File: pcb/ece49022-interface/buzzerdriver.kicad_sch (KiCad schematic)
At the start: 4 parts, among them Q1 C1815

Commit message: Interface
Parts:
- Q1: value C1815 -> KSC1815
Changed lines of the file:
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@@
 			)
 		)
-		(property "Value" "C1815"
+		(property "Value" "KSC1815"
 			(at 130.81 110.4899 0)
 			(effects
@@
 			)
 		)
-		(property "Description" "5399-C1815CT-ND"
+		(property "Description" "KSC1815YTA"
 			(at 125.73 109.22 0)
 			(effects

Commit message: footprint update
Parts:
- R2, R3: footprint (none) -> Resistor_SMD:R_0402_1005Metric
- renumbered Buzzer to Buzzer1
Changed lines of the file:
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@@
 		(dnp no)
 		(fields_autoplaced yes)
-		(property "Reference" "Buzzer"
+		(property "Reference" "Buzzer1"
 			(at 152.4 90.1699 90)
 			(effects
@@
 			(project "ece49022-interface"
 				(path "/ad062fbe-cbe6-4ffd-876d-97a59a1c7176/6d9997a2-880e-441e-bac1-2563afa1369d"
-					(reference "Buzzer")
+					(reference "Buzzer1")
 					(unit 1)
 				)
@@
 			)
 		)
-		(property "Footprint" ""
+		(property "Footprint" "Resistor_SMD:R_0402_1005Metric"
 			(at 127.254 91.186 90)
 			(effects
@@
 			)
 		)
-		(property "Footprint" ""
+		(property "Footprint" "Resistor_SMD:R_0402_1005Metric"
 			(at 108.204 108.204 90)
 			(effects

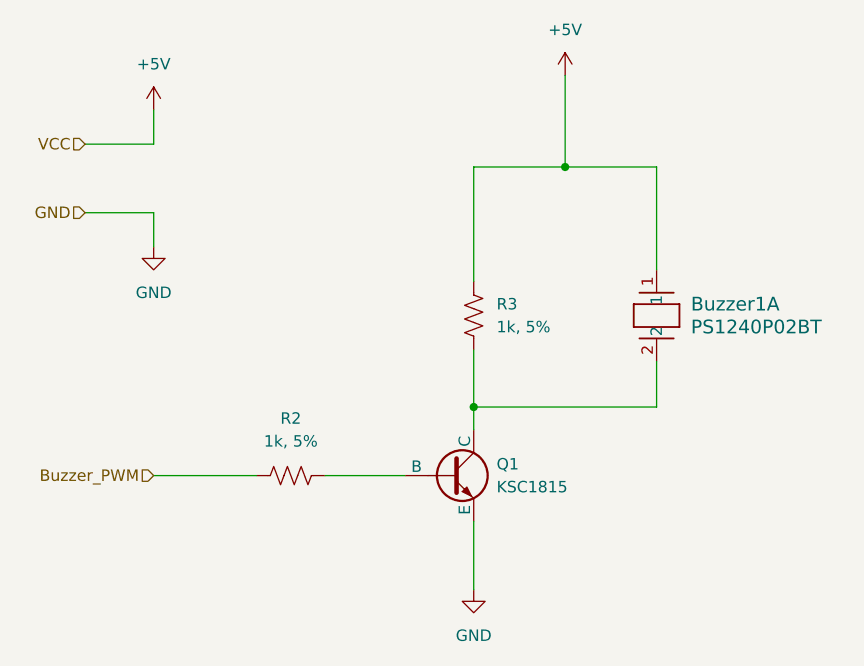
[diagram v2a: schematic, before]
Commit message: update buzzer and led
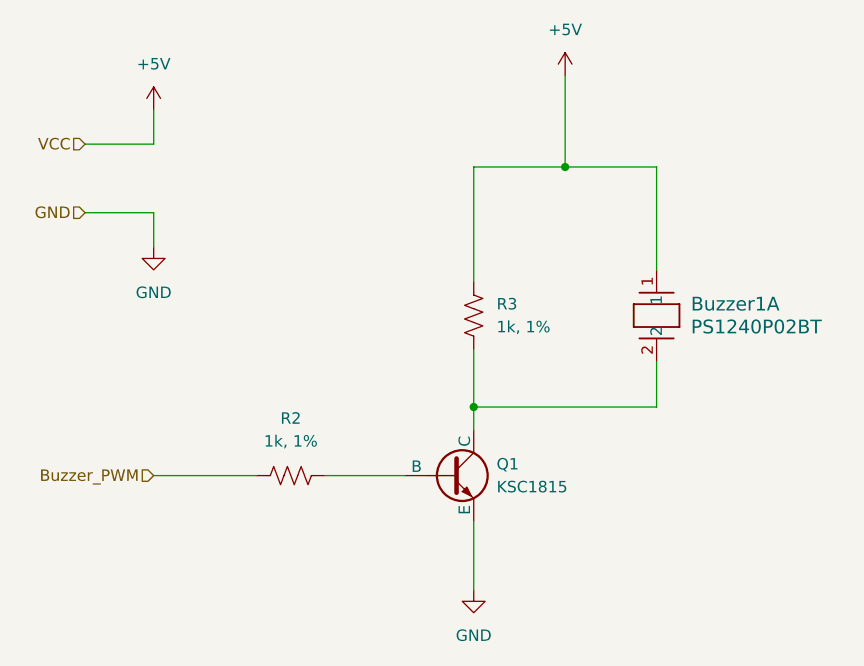
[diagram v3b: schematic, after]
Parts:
- Buzzer1: footprint XTAL_PS1240P02BT_TDK -> Buzzer_Beeper:Buzzer_TDK_PS1240P02BT_D12.2mm_H6.5mm
- Q1: footprint (none) -> Package_TO_SOT_THT:TO-92L_Inline_Wide
- R2, R3: value 1k, 5% -> 1k, 1%; footprint Resistor_SMD:R_0402_1005Metric -> Resistor_SMD:R_0402_1005Metric_Pad0.72x0.64mm_HandSolder
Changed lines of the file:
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@@
+	)
+	(symbol
+		(lib_id "Device:R_US")
+		(at 128.27 91.44 180)
+		(unit 1)
+		(exclude_from_sim no)
+		(in_bom yes)
+		(on_board yes)
+		(dnp no)
+		(fields_autoplaced yes)
+		(property "Reference" "R3"
+			(at 130.81 90.1699 0)
+			(effects
+				(font
+					(size 1.27 1.27)
+				)
+				(justify right)
+			)
+		)
+		(property "Value" "1k, 1%"
+			(at 130.81 92.7099 0)
+			(effects
+				(font
+					(size 1.27 1.27)
+				)
+				(justify right)
+			)
+		)
+		(property "Footprint" "Resistor_SMD:R_0402_1005Metric_Pad0.72x0.64mm_HandSolder"
+			(at 127.254 91.186 90)
+			(effects
+				(font
+					(size 1.27 1.27)
+				)
+				(hide yes)
+			)
+		)
+		(property "Datasheet" "https://yageogroup.com/content/datasheet/asset/file/PYU-RC_GROUP_51_ROHS_L"
+			(at 128.27 91.44 0)
+			(effects
+				(font
+					(size 1.27 1.27)
+				)
+				(hide yes)
+			)
+		)
+		(property "Description" "RC0402FR-071KL"
+			(at 128.27 91.44 0)
+			(effects
+				(font
+					(size 1.27 1.27)
+				)
+				(hide yes)
+			)
+		)
+		(pin "2"
+		)
+		(pin "1"
+		)
+		(instances
+			(project "ece49022-interface"
+				(path "/ad062fbe-cbe6-4ffd-876d-97a59a1c7176/6d9997a2-880e-441e-bac1-2563afa1369d"
+					(reference "R3")
+					(unit 1)
+				)
+			)
+		)
 	)
 	(symbol
@@
 			)
 		)
-		(property "Footprint" "XTAL_PS1240P02BT_TDK"
+		(property "Footprint" "Buzzer_Beeper:Buzzer_TDK_PS1240P02BT_D12.2mm_H6.5mm"
 			(at 148.59 86.36 0)
 			(effects
@@
 	(symbol
 		(lib_id "Device:R_US")
-		(at 128.27 91.44 180)
-		(unit 1)
-		(exclude_from_sim no)
-		(in_bom yes)
-		(on_board yes)
-		(dnp no)
-		(fields_autoplaced yes)
-		(property "Reference" "R3"
-			(at 130.81 90.1699 0)
-			(effects
-				(font
-					(size 1.27 1.27)
-				)
-				(justify right)
-			)
-		)
-		(property "Value" "1k, 5%"
-			(at 130.81 92.7099 0)
-			(effects
-				(font
-					(size 1.27 1.27)
-				)
-				(justify right)
-			)
-		)
-		(property "Footprint" "Resistor_SMD:R_0402_1005Metric"
-			(at 127.254 91.186 90)
-			(effects
-				(font
-					(size 1.27 1.27)
-				)
-				(hide yes)
-			)
-		)
-		(property "Datasheet" "~"
-			(at 128.27 91.44 0)
-			(effects
-				(font
-					(size 1.27 1.27)
-				)
-				(hide yes)
-			)
-		)
-		(property "Description" "RC0402JR-071KL"
-			(at 128.27 91.44 0)
-			(effects
-				(font
-					(size 1.27 1.27)
-				)
-				(hide yes)
-			)
-		)
-		(pin "2"
-		)
-		(pin "1"
-		)
-		(instances
-			(project "ece49022-interface"
-				(path "/ad062fbe-cbe6-4ffd-876d-97a59a1c7176/6d9997a2-880e-441e-bac1-2563afa1369d"
-					(reference "R3")
-					(unit 1)
-				)
-			)
-		)
-	)
-	(symbol
-		(lib_id "Device:R_US")
 		(at 107.95 109.22 90)
 		(unit 1)
@@
 			)
 		)
-		(property "Value" "1k, 5%"
+		(property "Value" "1k, 1%"
 			(at 107.95 105.41 90)
 			(effects
@@
 			)
 		)
-		(property "Footprint" "Resistor_SMD:R_0402_1005Metric"
+		(property "Footprint" "Resistor_SMD:R_0402_1005Metric_Pad0.72x0.64mm_HandSolder"
 			(at 108.204 108.204 90)
 			(effects
@@
 			)
 		)
-		(property "Datasheet" "~"
+		(property "Datasheet" "https://yageogroup.com/content/datasheet/asset/file/PYU-RC_GROUP_51_ROHS_L"
 			(at 107.95 109.22 0)
 			(effects
@@
 			)
 		)
-		(property "Description" "RC0402JR-071KL"
+		(property "Description" "RC0402FR-071KL"
 			(at 107.95 109.22 0)
 			(effects
@@
 			)
 		)
-		(property "Footprint" ""
+		(property "Footprint" "Package_TO_SOT_THT:TO-92L_Inline_Wide"
 			(at 189.23 109.22 0)
 			(effects
@@
 			)
 		)
-		(property "Datasheet" ""
+		(property "Datasheet" "https://www.onsemi.com/pdf/datasheet/ksc1815-d.pdf"
 			(at 189.23 109.22 0)
 			(effects
